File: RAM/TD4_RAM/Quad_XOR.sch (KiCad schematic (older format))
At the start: 2 parts, among them U2 74HC86

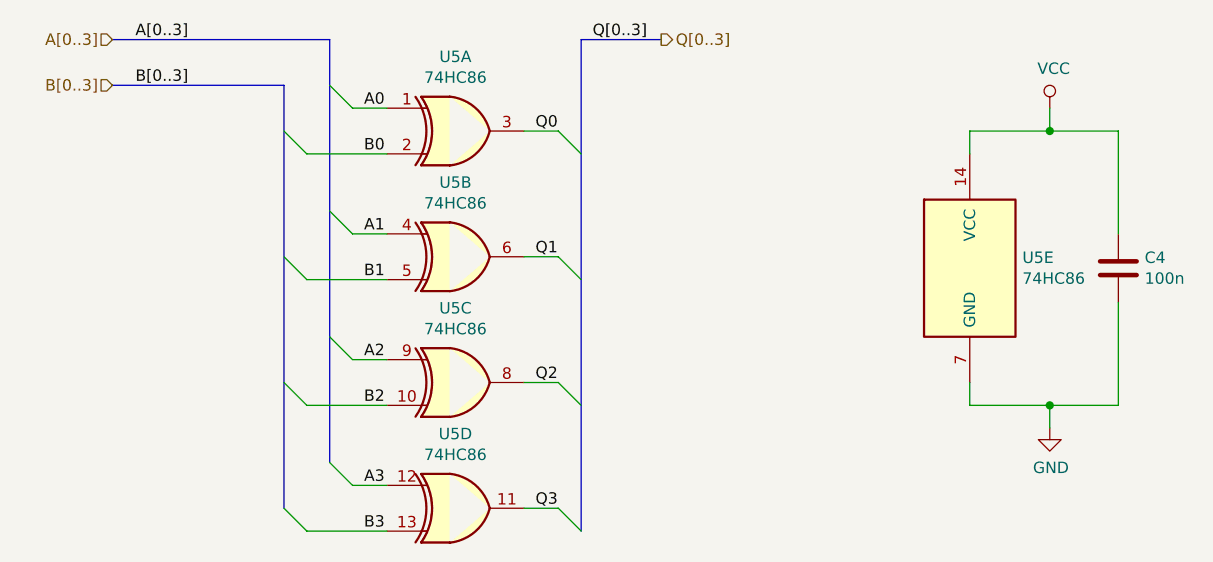
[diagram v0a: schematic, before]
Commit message: Added backplane connectors to all PCBs
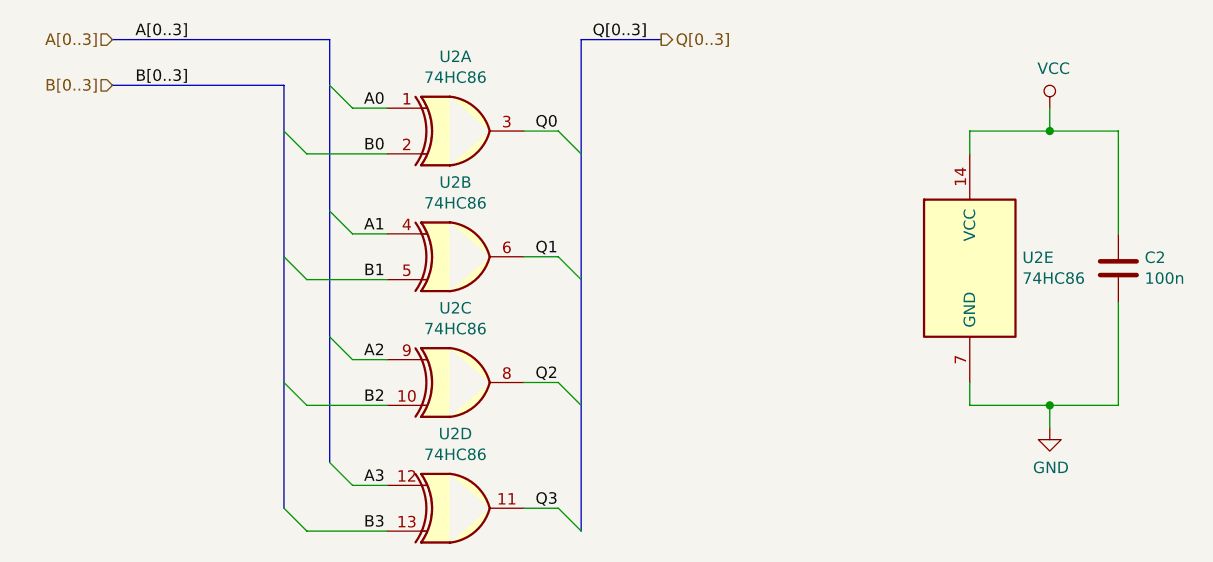
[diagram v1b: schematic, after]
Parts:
- C2: renamed from C1; footprint (none) -> Capacitor_SMD:C_0805_2012Metric
- U2: footprint (none) -> Package_SO:SOIC-14_3.9x8.7mm_P1.27mm
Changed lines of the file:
@@
 AR Path="/5C5DC05E/5CCDF31F/5C5DC2EE" Ref="U18"  Part="1"
 AR Path="/5C5DC05E/5CCE6007/5C5DC2EE" Ref="U19"  Part="1"
-F 0 "U5" H 4850 2925 50  0000 C CNN
+F 0 "U2" H 4850 2925 50  0000 C CNN
 F 1 "74HC86" H 4850 2834 50  0000 C CNN
-F 2 "" H 4850 2600 50  0001 C CNN
+F 2 "Package_SO:SOIC-14_3.9x8.7mm_P1.27mm" H 4850 2600 50  0001 C CNN
 F 3 "http://www.ti.com/lit/gpn/sn74HC86" H 4850 2600 50  0001 C CNN
 	1    4850 2600
@@
 AR Path="/5C5DC05E/5CCDF31F/5C5DC376" Ref="U18"  Part="2"
 AR Path="/5C5DC05E/5CCE6007/5C5DC376" Ref="U19"  Part="2"
-F 0 "U5" H 4850 3475 50  0000 C CNN
+F 0 "U2" H 4850 3475 50  0000 C CNN
 F 1 "74HC86" H 4850 3384 50  0000 C CNN
-F 2 "" H 4850 3150 50  0001 C CNN
+F 2 "Package_SO:SOIC-14_3.9x8.7mm_P1.27mm" H 4850 3150 50  0001 C CNN
 F 3 "http://www.ti.com/lit/gpn/sn74HC86" H 4850 3150 50  0001 C CNN
 	2    4850 3150
@@
 AR Path="/5C5DC05E/5CCDF31F/5C5DC396" Ref="U18"  Part="3"
 AR Path="/5C5DC05E/5CCE6007/5C5DC396" Ref="U19"  Part="3"
-F 0 "U5" H 4850 4025 50  0000 C CNN
+F 0 "U2" H 4850 4025 50  0000 C CNN
 F 1 "74HC86" H 4850 3934 50  0000 C CNN
-F 2 "" H 4850 3700 50  0001 C CNN
+F 2 "Package_SO:SOIC-14_3.9x8.7mm_P1.27mm" H 4850 3700 50  0001 C CNN
 F 3 "http://www.ti.com/lit/gpn/sn74HC86" H 4850 3700 50  0001 C CNN
 	3    4850 3700
@@
 AR Path="/5C5DC05E/5CCDF31F/5C5DC3D2" Ref="U18"  Part="4"
 AR Path="/5C5DC05E/5CCE6007/5C5DC3D2" Ref="U19"  Part="4"
-F 0 "U5" H 4850 4575 50  0000 C CNN
+F 0 "U2" H 4850 4575 50  0000 C CNN
 F 1 "74HC86" H 4850 4484 50  0000 C CNN
-F 2 "" H 4850 4250 50  0001 C CNN
+F 2 "Package_SO:SOIC-14_3.9x8.7mm_P1.27mm" H 4850 4250 50  0001 C CNN
 F 3 "http://www.ti.com/lit/gpn/sn74HC86" H 4850 4250 50  0001 C CNN
 	4    4850 4250
@@
 AR Path="/5C5DC05E/5CCDF31F/5C5DC430" Ref="U18"  Part="5"
 AR Path="/5C5DC05E/5CCE6007/5C5DC430" Ref="U19"  Part="5"
-F 0 "U5" H 7330 3246 50  0000 L CNN
+F 0 "U2" H 7330 3246 50  0000 L CNN
 F 1 "74HC86" H 7330 3155 50  0000 L CNN
-F 2 "" H 7100 3200 50  0001 C CNN
+F 2 "Package_SO:SOIC-14_3.9x8.7mm_P1.27mm" H 7100 3200 50  0001 C CNN
 F 3 "http://www.ti.com/lit/gpn/sn74HC86" H 7100 3200 50  0001 C CNN
 	5    7100 3200
@@
 $EndComp
 $Comp
-L Device:C C1
+L Device:C C2
 U 1 1 5C5DC564
 P 7750 3200
-AR Path="/5C5DC05E/5C5DC213/5C5DC564" Ref="C1"  Part="1"
+AR Path="/5C5DC05E/5C5DC213/5C5DC564" Ref="C2"  Part="1"
 AR Path="/5C5DC05E/5C5E95C7/5C5DC564" Ref="C?"  Part="1"
 AR Path="/5C5DC05E/5C5E965E/5C5DC564" Ref="C?"  Part="1"
@@
 AR Path="/5C5DC05E/5C8E6B2E/5C5DC564" Ref="C?"  Part="1"
 AR Path="/5C5DC05E/5C8E6B33/5C5DC564" Ref="C?"  Part="1"
-AR Path="/5C5DC05E/5CC7FE6F/5C5DC564" Ref="C4"  Part="1"
-AR Path="/5C5DC05E/5CC86B57/5C5DC564" Ref="C5"  Part="1"
-AR Path="/5C5DC05E/5CC8D83F/5C5DC564" Ref="C6"  Part="1"
-AR Path="/5C5DC05E/5CC94527/5C5DC564" Ref="C7"  Part="1"
-AR Path="/5C5DC05E/5CC9B20F/5C5DC564" Ref="C8"  Part="1"
-AR Path="/5C5DC05E/5CCA1EF7/5C5DC564" Ref="C9"  Part="1"
-AR Path="/5C5DC05E/5CCA8BDF/5C5DC564" Ref="C10"  Part="1"
-AR Path="/5C5DC05E/5CCAF8C7/5C5DC564" Ref="C11"  Part="1"
-AR Path="/5C5DC05E/5CCB65AF/5C5DC564" Ref="C12"  Part="1"
-AR Path="/5C5DC05E/5CCBD297/5C5DC564" Ref="C13"  Part="1"
-AR Path="/5C5DC05E/5CCC3F7F/5C5DC564" Ref="C14"  Part="1"
-AR Path="/5C5DC05E/5CCCAC67/5C5DC564" Ref="C15"  Part="1"
+AR Path="/5C5DC05E/5CC7FE6F/5C5DC564" Ref="C5"  Part="1"
+AR Path="/5C5DC05E/5CC86B57/5C5DC564" Ref="C6"  Part="1"
+AR Path="/5C5DC05E/5CC8D83F/5C5DC564" Ref="C7"  Part="1"
+AR Path="/5C5DC05E/5CC94527/5C5DC564" Ref="C8"  Part="1"
+AR Path="/5C5DC05E/5CC9B20F/5C5DC564" Ref="C9"  Part="1"
+AR Path="/5C5DC05E/5CCA1EF7/5C5DC564" Ref="C10"  Part="1"
+AR Path="/5C5DC05E/5CCA8BDF/5C5DC564" Ref="C11"  Part="1"
+AR Path="/5C5DC05E/5CCAF8C7/5C5DC564" Ref="C12"  Part="1"
+AR Path="/5C5DC05E/5CCB65AF/5C5DC564" Ref="C13"  Part="1"
+AR Path="/5C5DC05E/5CCBD297/5C5DC564" Ref="C14"  Part="1"
+AR Path="/5C5DC05E/5CCC3F7F/5C5DC564" Ref="C15"  Part="1"
+AR Path="/5C5DC05E/5CCCAC67/5C5DC564" Ref="C16"  Part="1"
 AR Path="/5C5DC05E/5CCD194F/5C5DC564" Ref="C?"  Part="1"
-AR Path="/5C5DC05E/5CCD8637/5C5DC564" Ref="C16"  Part="1"
-AR Path="/5C5DC05E/5CCDF31F/5C5DC564" Ref="C17"  Part="1"
-AR Path="/5C5DC05E/5CCE6007/5C5DC564" Ref="C18"  Part="1"
-F 0 "C4" H 7865 3246 50  0000 L CNN
+AR Path="/5C5DC05E/5CCD8637/5C5DC564" Ref="C17"  Part="1"
+AR Path="/5C5DC05E/5CCDF31F/5C5DC564" Ref="C18"  Part="1"
+AR Path="/5C5DC05E/5CCE6007/5C5DC564" Ref="C19"  Part="1"
+F 0 "C2" H 7865 3246 50  0000 L CNN
 F 1 "100n" H 7865 3155 50  0000 L CNN
-F 2 "" H 7788 3050 50  0001 C CNN
+F 2 "Capacitor_SMD:C_0805_2012Metric" H 7788 3050 50  0001 C CNN
 F 3 "~" H 7750 3200 50  0001 C CNN
 	1    7750 3200
@@
 Q[0..3]
 $Comp
-L power:GND #PWR04
+L power:GND #PWR019
 U 1 1 5C5DF5EB
 P 7450 3900
-AR Path="/5C5DC05E/5C5DC213/5C5DF5EB" Ref="#PWR04"  Part="1"
+AR Path="/5C5DC05E/5C5DC213/5C5DF5EB" Ref="#PWR019"  Part="1"
 AR Path="/5C5DC05E/5C5E95C7/5C5DF5EB" Ref="#PWR?"  Part="1"
 AR Path="/5C5DC05E/5C5E965E/5C5DF5EB" Ref="#PWR?"  Part="1"
@@
 AR Path="/5C5DC05E/5C8E6B2E/5C5DF5EB" Ref="#PWR?"  Part="1"
 AR Path="/5C5DC05E/5C8E6B33/5C5DF5EB" Ref="#PWR?"  Part="1"
-AR Path="/5C5DC05E/5CC7FE6F/5C5DF5EB" Ref="#PWR042"  Part="1"
-AR Path="/5C5DC05E/5CC86B57/5C5DF5EB" Ref="#PWR044"  Part="1"
-AR Path="/5C5DC05E/5CC8D83F/5C5DF5EB" Ref="#PWR046"  Part="1"
-AR Path="/5C5DC05E/5CC94527/5C5DF5EB" Ref="#PWR048"  Part="1"
-AR Path="/5C5DC05E/5CC9B20F/5C5DF5EB" Ref="#PWR050"  Part="1"
-AR Path="/5C5DC05E/5CCA1EF7/5C5DF5EB" Ref="#PWR052"  Part="1"
-AR Path="/5C5DC05E/5CCA8BDF/5C5DF5EB" Ref="#PWR054"  Part="1"
-AR Path="/5C5DC05E/5CCAF8C7/5C5DF5EB" Ref="#PWR056"  Part="1"
-AR Path="/5C5DC05E/5CCB65AF/5C5DF5EB" Ref="#PWR058"  Part="1"
-AR Path="/5C5DC05E/5CCBD297/5C5DF5EB" Ref="#PWR060"  Part="1"
-AR Path="/5C5DC05E/5CCC3F7F/5C5DF5EB" Ref="#PWR062"  Part="1"
-AR Path="/5C5DC05E/5CCCAC67/5C5DF5EB" Ref="#PWR064"  Part="1"
+AR Path="/5C5DC05E/5CC7FE6F/5C5DF5EB" Ref="#PWR057"  Part="1"
+AR Path="/5C5DC05E/5CC86B57/5C5DF5EB" Ref="#PWR059"  Part="1"
+AR Path="/5C5DC05E/5CC8D83F/5C5DF5EB" Ref="#PWR061"  Part="1"
+AR Path="/5C5DC05E/5CC94527/5C5DF5EB" Ref="#PWR063"  Part="1"
+AR Path="/5C5DC05E/5CC9B20F/5C5DF5EB" Ref="#PWR065"  Part="1"
+AR Path="/5C5DC05E/5CCA1EF7/5C5DF5EB" Ref="#PWR067"  Part="1"
+AR Path="/5C5DC05E/5CCA8BDF/5C5DF5EB" Ref="#PWR069"  Part="1"
+AR Path="/5C5DC05E/5CCAF8C7/5C5DF5EB" Ref="#PWR071"  Part="1"
+AR Path="/5C5DC05E/5CCB65AF/5C5DF5EB" Ref="#PWR073"  Part="1"
+AR Path="/5C5DC05E/5CCBD297/5C5DF5EB" Ref="#PWR075"  Part="1"
+AR Path="/5C5DC05E/5CCC3F7F/5C5DF5EB" Ref="#PWR077"  Part="1"
+AR Path="/5C5DC05E/5CCCAC67/5C5DF5EB" Ref="#PWR079"  Part="1"
 AR Path="/5C5DC05E/5CCD194F/5C5DF5EB" Ref="#PWR?"  Part="1"
-AR Path="/5C5DC05E/5CCD8637/5C5DF5EB" Ref="#PWR066"  Part="1"
-AR Path="/5C5DC05E/5CCDF31F/5C5DF5EB" Ref="#PWR068"  Part="1"
-AR Path="/5C5DC05E/5CCE6007/5C5DF5EB" Ref="#PWR070"  Part="1"
-F 0 "#PWR042" H 7450 3650 50  0001 C CNN
+AR Path="/5C5DC05E/5CCD8637/5C5DF5EB" Ref="#PWR081"  Part="1"
+AR Path="/5C5DC05E/5CCDF31F/5C5DF5EB" Ref="#PWR083"  Part="1"
+AR Path="/5C5DC05E/5CCE6007/5C5DF5EB" Ref="#PWR085"  Part="1"
+F 0 "#PWR019" H 7450 3650 50  0001 C CNN
 F 1 "GND" H 7455 3727 50  0000 C CNN
 F 2 "" H 7450 3900 50  0001 C CNN
@@
 	7100 2600 7450 2600
 $Comp
-L power:VCC #PWR03
+L power:VCC #PWR018
 U 1 1 5C5E1083
 P 7450 2500
-AR Path="/5C5DC05E/5C5DC213/5C5E1083" Ref="#PWR03"  Part="1"
+AR Path="/5C5DC05E/5C5DC213/5C5E1083" Ref="#PWR018"  Part="1"
 AR Path="/5C5DC05E/5C5E95C7/5C5E1083" Ref="#PWR?"  Part="1"
 AR Path="/5C5DC05E/5C5E965E/5C5E1083" Ref="#PWR?"  Part="1"
@@
 AR Path="/5C5DC05E/5C8E6B2E/5C5E1083" Ref="#PWR?"  Part="1"
 AR Path="/5C5DC05E/5C8E6B33/5C5E1083" Ref="#PWR?"  Part="1"
-AR Path="/5C5DC05E/5CC7FE6F/5C5E1083" Ref="#PWR041"  Part="1"
-AR Path="/5C5DC05E/5CC86B57/5C5E1083" Ref="#PWR043"  Part="1"
-AR Path="/5C5DC05E/5CC8D83F/5C5E1083" Ref="#PWR045"  Part="1"
-AR Path="/5C5DC05E/5CC94527/5C5E1083" Ref="#PWR047"  Part="1"
-AR Path="/5C5DC05E/5CC9B20F/5C5E1083" Ref="#PWR049"  Part="1"
-AR Path="/5C5DC05E/5CCA1EF7/5C5E1083" Ref="#PWR051"  Part="1"
-AR Path="/5C5DC05E/5CCA8BDF/5C5E1083" Ref="#PWR053"  Part="1"
-AR Path="/5C5DC05E/5CCAF8C7/5C5E1083" Ref="#PWR055"  Part="1"
-AR Path="/5C5DC05E/5CCB65AF/5C5E1083" Ref="#PWR057"  Part="1"
-AR Path="/5C5DC05E/5CCBD297/5C5E1083" Ref="#PWR059"  Part="1"
-AR Path="/5C5DC05E/5CCC3F7F/5C5E1083" Ref="#PWR061"  Part="1"
-AR Path="/5C5DC05E/5CCCAC67/5C5E1083" Ref="#PWR063"  Part="1"
+AR Path="/5C5DC05E/5CC7FE6F/5C5E1083" Ref="#PWR056"  Part="1"
+AR Path="/5C5DC05E/5CC86B57/5C5E1083" Ref="#PWR058"  Part="1"
+AR Path="/5C5DC05E/5CC8D83F/5C5E1083" Ref="#PWR060"  Part="1"
+AR Path="/5C5DC05E/5CC94527/5C5E1083" Ref="#PWR062"  Part="1"
+AR Path="/5C5DC05E/5CC9B20F/5C5E1083" Ref="#PWR064"  Part="1"
+AR Path="/5C5DC05E/5CCA1EF7/5C5E1083" Ref="#PWR066"  Part="1"
+AR Path="/5C5DC05E/5CCA8BDF/5C5E1083" Ref="#PWR068"  Part="1"
+AR Path="/5C5DC05E/5CCAF8C7/5C5E1083" Ref="#PWR070"  Part="1"
+AR Path="/5C5DC05E/5CCB65AF/5C5E1083" Ref="#PWR072"  Part="1"
+AR Path="/5C5DC05E/5CCBD297/5C5E1083" Ref="#PWR074"  Part="1"
+AR Path="/5C5DC05E/5CCC3F7F/5C5E1083" Ref="#PWR076"  Part="1"
+AR Path="/5C5DC05E/5CCCAC67/5C5E1083" Ref="#PWR078"  Part="1"
 AR Path="/5C5DC05E/5CCD194F/5C5E1083" Ref="#PWR?"  Part="1"
-AR Path="/5C5DC05E/5CCD8637/5C5E1083" Ref="#PWR065"  Part="1"
-AR Path="/5C5DC05E/5CCDF31F/5C5E1083" Ref="#PWR067"  Part="1"
-AR Path="/5C5DC05E/5CCE6007/5C5E1083" Ref="#PWR069"  Part="1"
-F 0 "#PWR041" H 7450 2350 50  0001 C CNN
+AR Path="/5C5DC05E/5CCD8637/5C5E1083" Ref="#PWR080"  Part="1"
+AR Path="/5C5DC05E/5CCDF31F/5C5E1083" Ref="#PWR082"  Part="1"
+AR Path="/5C5DC05E/5CCE6007/5C5E1083" Ref="#PWR084"  Part="1"
+F 0 "#PWR018" H 7450 2350 50  0001 C CNN
 F 1 "VCC" H 7467 2673 50  0000 C CNN
 F 2 "" H 7450 2500 50  0001 C CNN
